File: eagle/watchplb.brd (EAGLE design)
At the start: 100 x 80 mm, 141 parts, among them IC1 SAM-M8Q, IC2 BM70BLES1FC2-0B03AA, Q1 8MHz / LFXTAL020423Reel, Q2 BC817-25SMD, Q3 DMN3023L-7, Q4 16MHz_LFXTAL051370Reel, U1 MCP111-XXXXX/TO, U2 STM32L073RZ, U3 MCP2200-I/SS, U4 TPD3E001DRLR

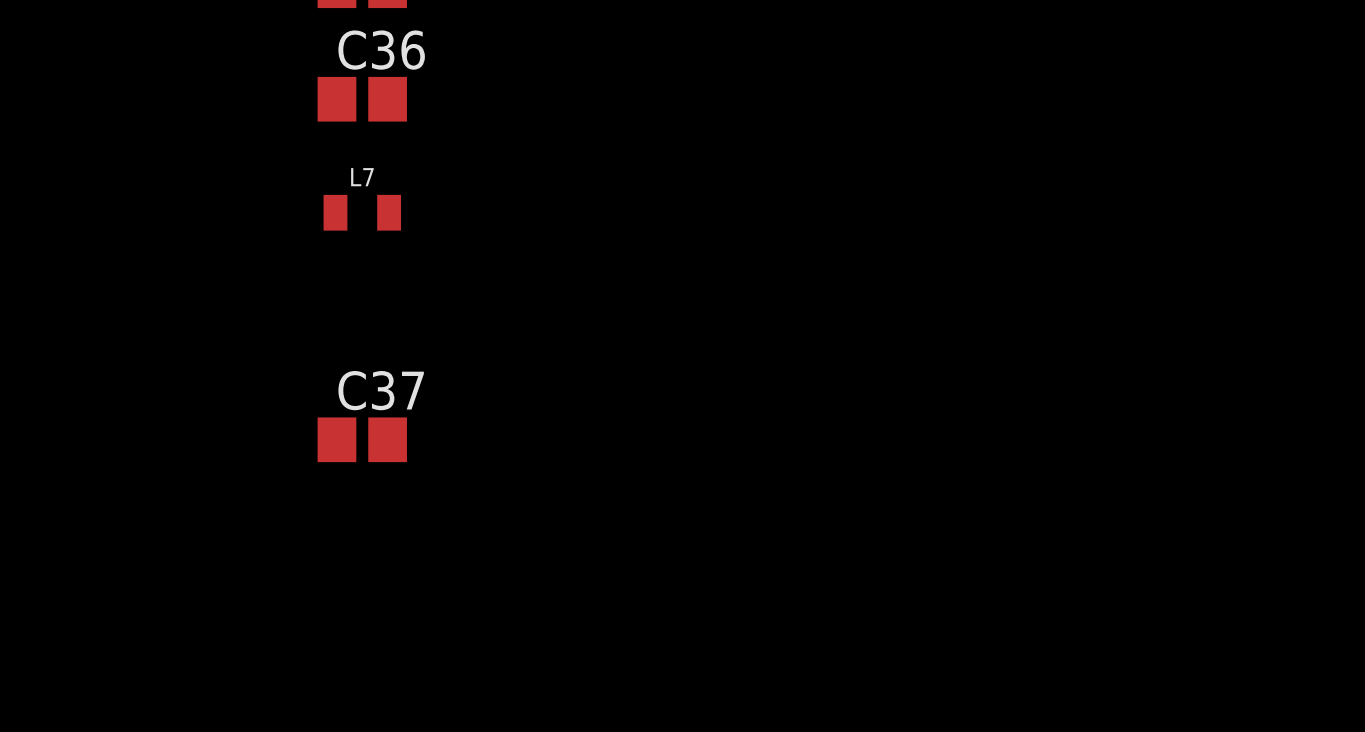
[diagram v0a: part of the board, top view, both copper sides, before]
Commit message: added rf amp and sma connector, reorganised for better pdf page ordering
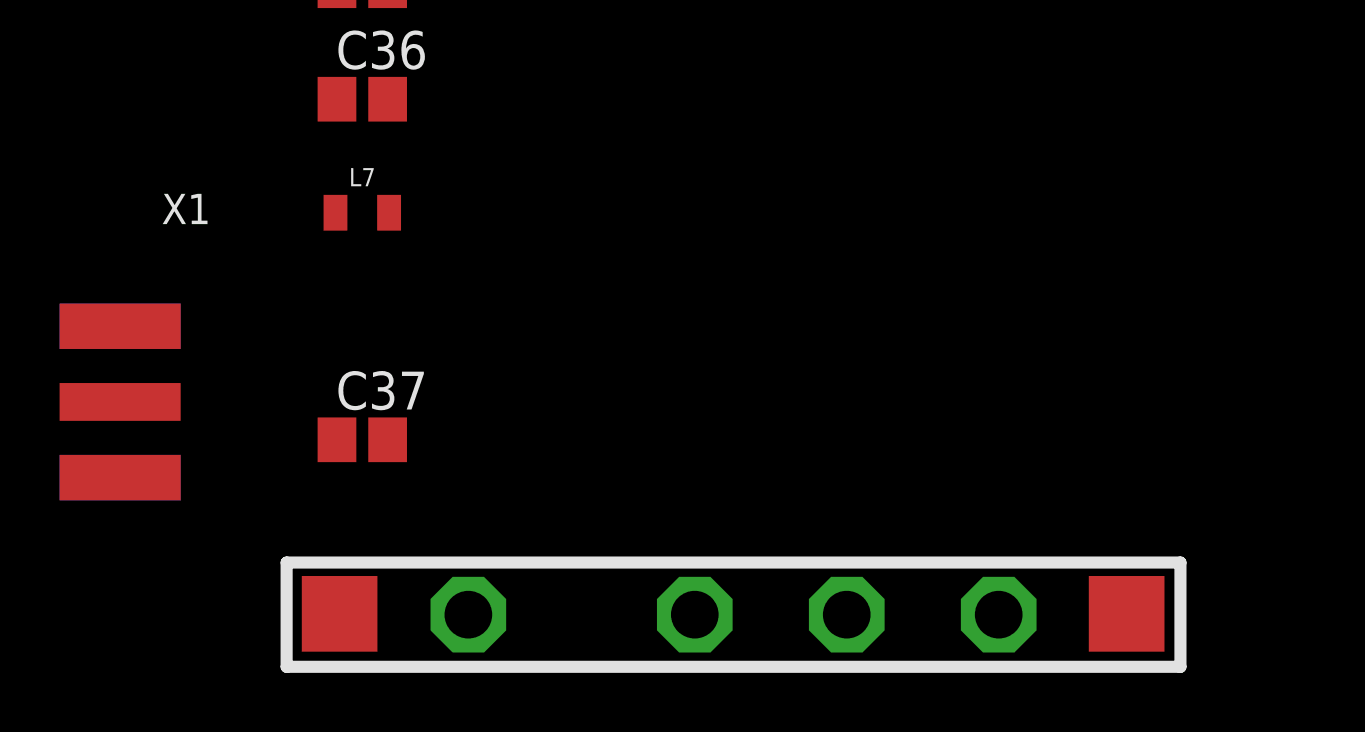
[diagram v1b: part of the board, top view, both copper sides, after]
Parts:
- added U$2: RA07H4047M, Hick:RA07H4047M
- added X1: (no value), adafruit:SMA_EDGELAUNCH
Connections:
- removed net N$38: C24.2, U$1.15
- new net +12V: U$2.2
- new net RF_SIGNAL_AMPLIFIED: U$2.4, X1.P
- net +3V3: now also C24.2, U$1.15, U$2.3
- net GND: now also U$2.5_L, U$2.5_R, X1.GND@1, X1.GND@2, X1.GND@3, X1.GND@4
- net RF_SIGNAL: now also U$2.1
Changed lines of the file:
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@@
 </element>
 <element name="C37" library="resistor" package="C0805" value="" x="-135.89" y="-843.28"/>
+<element name="U$2" library="Hick" package="RA07H4047M" value="RA07H4047M" x="-138.43" y="-850.9"/>
+<element name="X1" library="adafruit" package="SMA_EDGELAUNCH" value="" x="-146.05" y="-842.01"/>
 </elements>
 <signals>
@@
 <contactref element="3V3" pad="TP"/>
 <contactref element="Q2" pad="C"/>
+<contactref element="U$2" pad="3"/>
+<contactref element="U$1" pad="15"/>
+<contactref element="C24" pad="2"/>
 <wire x1="-74.08" y1="-193.04" x2="-67.31" y2="-185.42" width="0" layer="19" extent="1-1"/>
 <wire x1="-81.09" y1="-216.13" x2="-74.08" y2="-193.04" width="0" layer="19" extent="1-1"/>
@@
 <wire x1="-121.92" y1="-521.97" x2="-111.44" y2="-377.19" width="0" layer="19" extent="1-1"/>
 <wire x1="-135.89" y1="-646.6" x2="-121.92" y2="-521.97" width="0" layer="19" extent="1-1"/>
+<wire x1="-135.62" y1="-672.57" x2="-135.89" y2="-646.6" width="0" layer="19" extent="1-1"/>
+<wire x1="-135.04" y1="-698.5" x2="-135.62" y2="-672.57" width="0" layer="19" extent="1-1"/>
+<wire x1="-119.63" y1="-849.15" x2="-135.04" y2="-698.5" width="0" layer="19" extent="1-1"/>
 </signal>
 <signal name="GPS_RXD">
@@
 <contactref element="C36" pad="1"/>
 <contactref element="C37" pad="1"/>
+<contactref element="X1" pad="GND@2"/>
+<contactref element="X1" pad="GND@1"/>
+<contactref element="X1" pad="GND@4"/>
+<contactref element="X1" pad="GND@3"/>
+<contactref element="U$2" pad="5_L"/>
+<contactref element="U$2" pad="5_R"/>
 <wire x1="-74.08" y1="-166.37" x2="-74.08" y2="-172.72" width="0" layer="19" extent="1-1"/>
 <wire x1="-74.93" y1="-185.42" x2="-74.08" y2="-172.72" width="0" layer="19" extent="1-1"/>
@@
 <wire x1="-136.79" y1="-820.42" x2="-136.74" y2="-816.61" width="0" layer="19" extent="1-1"/>
 <wire x1="-136.74" y1="-831.85" x2="-136.79" y2="-820.42" width="0" layer="19" extent="1-1"/>
-<wire x1="-136.74" y1="-843.28" x2="-136.74" y2="-831.85" width="0" layer="19" extent="1-1"/>
+<wire x1="-144.018" y1="-839.47" x2="-136.74" y2="-831.85" width="0" layer="19" extent="1-1"/>
+<wire x1="-144.018" y1="-839.47" x2="-144.018" y2="-839.47" width="0" layer="19" extent="1-16"/>
+<wire x1="-144.018" y1="-844.55" x2="-144.018" y2="-839.47" width="0" layer="19" extent="1-1"/>
+<wire x1="-144.018" y1="-844.55" x2="-144.018" y2="-844.55" width="0" layer="19" extent="1-16"/>
+<wire x1="-136.74" y1="-843.28" x2="-144.018" y2="-844.55" width="0" layer="19" extent="1-1"/>
+<wire x1="-136.652" y1="-849.122" x2="-136.74" y2="-843.28" width="0" layer="19" extent="1-1"/>
+<wire x1="-110.236" y1="-849.122" x2="-136.652" y2="-849.122" width="0" layer="19" extent="1-1"/>
 </signal>
 <signal name="BT_NRST">
@@
 <wire x1="-136.84" y1="-661.67" x2="-134.94" y2="-668.02" width="0" layer="19" extent="1-1"/>
 <wire x1="-136.84" y1="-648.8" x2="-136.84" y2="-661.67" width="0" layer="19" extent="1-1"/>
-</signal>
-<signal name="N$38">
-<contactref element="U$1" pad="15"/>
-<contactref element="C24" pad="2"/>
-<wire x1="-135.62" y1="-672.57" x2="-135.04" y2="-698.5" width="0" layer="19" extent="1-1"/>
 </signal>
 <signal name="INT_POWER">
@@
 <contactref element="L7" pad="2"/>
 <contactref element="C37" pad="2"/>
+<contactref element="U$2" pad="1"/>
+<wire x1="-135.04" y1="-843.28" x2="-132.33" y2="-849.15" width="0" layer="19" extent="1-1"/>
 <wire x1="-134.99" y1="-835.66" x2="-135.04" y2="-843.28" width="0" layer="19" extent="1-1"/>
+</signal>
+<signal name="RF_SIGNAL_AMPLIFIED">
+<contactref element="U$2" pad="4"/>
+<contactref element="X1" pad="P"/>
+<wire x1="-114.53" y1="-849.15" x2="-144.018" y2="-842.01" width="0" layer="19" extent="1-1"/>
+</signal>
+<signal name="+12V">
+<contactref element="U$2" pad="2"/>
 </signal>
 </signals>
 </board>
 </drawing>
+<compatibility>
+<note version="6.3" minversion="6.2.2" severity="warning">
+Since Version 6.2.2 text objects can contain more than one line,
+which will not be processed correctly with this version.
+</note>
+</compatibility>
 </eagle>

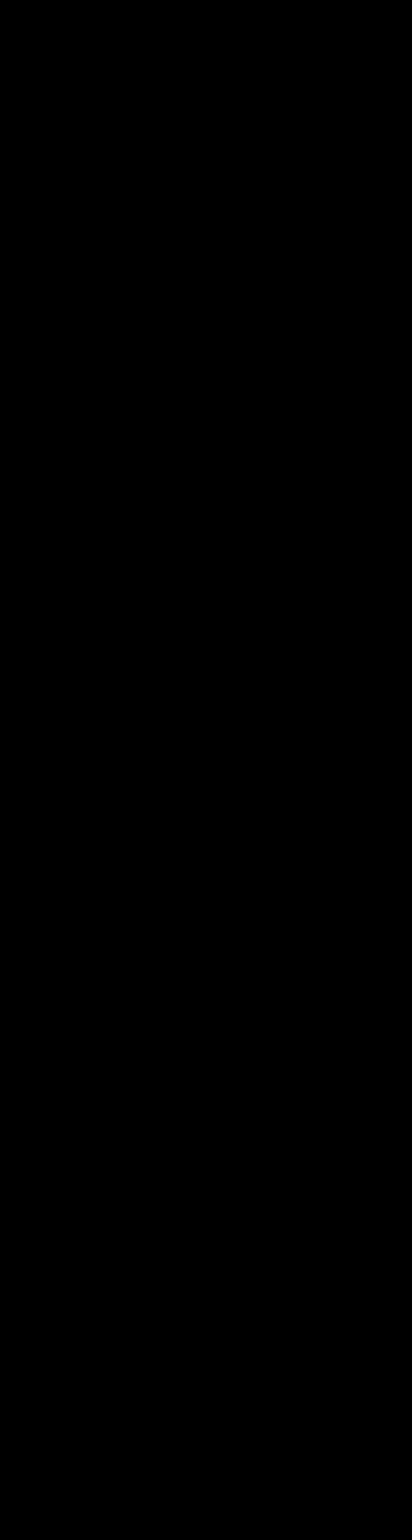
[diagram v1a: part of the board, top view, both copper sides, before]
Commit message: added battery protection circuit
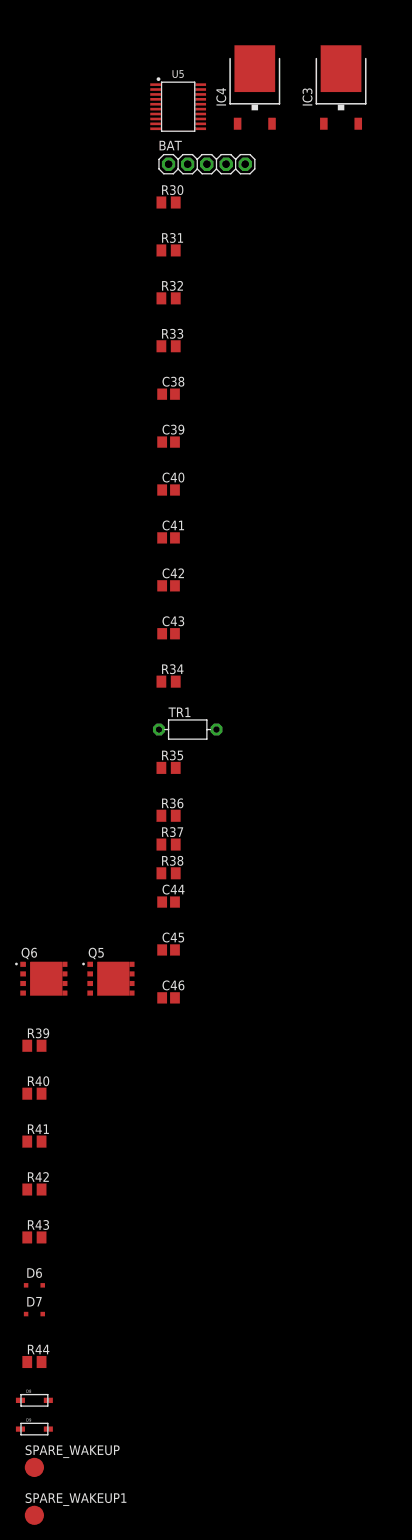
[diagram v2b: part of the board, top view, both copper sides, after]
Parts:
- added BAT: (no value), pinhead:1X05
- added C38, C39, C40, C41, C44, C45, C46: 100nF, resistor:C0805
- added C42, C43: 1uF, resistor:C0805
- added D6: Zener 16V MMSZ5246BS-7-F, diode-1:SOD323-R
- added D7: 100V, BAS16J,135, diode-1:SOD323-R
- added D8, D9: (no value), adafruit:SOD-123
- added IC3: LM1117DTX-ADJ-12V, lm1117:TO252
- added IC4: LM1117DTX-ADJ-3V3, lm1117:TO252
- added Q5, Q6: CSD18534Q5A, CSD18534Q5A:TRANS_CSD18534Q5A
- added R30, R31, R32, R33, R34: 1k, resistor:M0805
- added R35: 10k, resistor:M0805
- added R36: 20mR, resistor:M0805
- added R37, R38: 100R, resistor:M0805
- added R39: 10M, resistor:M0805
- added R40, R43: 5k1, resistor:M0805
- added R41: 3M3, resistor:M0805
- added R42: 1M, resistor:M0805
- added R44: 470k, resistor:M0805
- added SPARE_WAKEUP, SPARE_WAKEUP1: PTR1B2,54, testpad:B2,54
- added TR1: NTC 103AT, discrete:R-7,5
- added U5: BQ7790504, chips:TSSOP-20/6MM
- R10, R11, R14, R15, R18, R19, R20, R21, R22: value 220R -> 470R
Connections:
- removed net V+: D1.C, JP2.1
- new net BAT_PACK_GND: BAT.5, C38.2, C39.2, C40.2, C41.2, C42.1, C43.2, C44.1, C46.2, R36.2, R37.2, TR1.1, U5.18, U5.19, U5.20, U5.8
- new net BAT_PACK_NEG: D6.A, Q6.1, Q6.2, Q6.3, R41.1, R44.2
- new net BAT_PACK_POS: BAT.1, R30.1, R34.1
- new net N$38: R35.2, TR1.2, U5.15
- new net N$46: D6.C, D7.C, Q6.4, R41.2, R42.1
- new net N$47: BAT.2, R31.1
- new net N$48: BAT.3, R32.1
- new net N$49: BAT.4, R33.1
- new net N$50: C39.1, R33.2, U5.7
- new net N$51: C40.1, R32.2, U5.6
- new net N$52: C41.1, R31.2, U5.5
- new net N$53: C38.1, R30.2, U5.3, U5.4
- new net N$54: C43.1, R34.2, U5.1
- new net N$55: Q5.1, Q5.2, Q5.3, R36.1, R38.2, R39.2
- new net N$56: C42.2, U5.17, U5.2
- new net N$57: C45.2, C46.1, R38.1, U5.10
- new net N$58: C44.2, C45.1, R37.1, U5.9
- new net N$59: Q5.5, Q5.6, Q5.7, Q5.8, Q6.5, Q6.6, Q6.7, Q6.8
- new net N$60: R35.1, U5.16
- new net N$62: Q5.4, R39.1, R40.1
- new net N$63: R40.2, U5.11
- new net N$64: D7.A, R42.2, R43.2
- new net N$65: R43.1, U5.13
- new net N$66: R44.1, U5.14
- new net N$67: D8.A, SPARE_WAKEUP1.TP
- new net N$68: D9.A, SPARE_WAKEUP.TP
- net +3V3: now also D1.C, JP2.1
- net MCU_WAKEUP: now also D8.C, D9.C

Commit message: added calculations as excel file and battery charge circuitry in schematic
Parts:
- removed X1: (no value), adafruit:SMA_EDGELAUNCH
- added C47, C49: 100nF, resistor:C0805
- added C48, C51, C52: 22uF 80-EDK226M050A9GAA, rcl:PANASONIC_E
- added C50: 4.7uF, resistor:C0805
- added D10: MBRS330T3, diode:SMC
- added J3: BNCPTH, SparkFun-Connectors:BNC
- added J4: (no value), SparkFun-Connectors:USB-B-MICRO-SMD
- added L8: CTX10-4A-R, CTX10-4A-R:INDM115115X635N
- added Q7: DMN3023L-7, transistor-small-signal:SOT23
- added R45: 330, resistor:M0805
- added R46: 910R, resistor:M0805
- added R47, R49: 10k, resistor:M0805
- added R48: 330k, resistor:M0805
- added R50: 0.25R, resistor:M0805
- added R51: 120k, resistor:M0805
- added R52: 12k4, resistor:M0805
- added U$3: LT1513, Hick:TO220-7
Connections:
- removed net BAT_PACK_NEG: D6.A, Q6.1, Q6.2, Q6.3, R41.1, R44.2
- new net N$61: C50.2, L8.2, U$3.5
- new net N$69: C48.+, J4.VBUS, L8.1, U$3.7
- new net N$70: L8.3, R49.2, R50.2
- new net N$71: C47.2, R45.2
- new net N$72: R45.1, U$3.1
- new net N$73: Q7.3, R46.1
- new net N$74: R46.2, R47.2, R48.1
- new net N$75: C50.1, D10.A, L8.4
- new net N$76: C49.2, R48.2, R49.1, U$3.3
- new net N$77: R51.1, R52.2, U$3.2
- new net S/S: U$3.6
- net +3V3: now also R47.1
- net BAT_PACK_POS: now also C51.+, C52.+, D10.C, R51.2
- net GND: now also C47.1, C48.-, C49.1, C51.-, C52.-, D6.A, J3.GND, J4.GND, J4.SHIELD1, J4.SHIELD2, J4.SHIELD3, Q6.1, Q6.2, Q6.3, Q7.2, R41.1, R44.2, R50.1, R52.1, U$3.4; no longer X1.GND@1, X1.GND@2, X1.GND@3, X1.GND@4
- net RF_SIGNAL_AMPLIFIED: now also J3.S; no longer X1.P

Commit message: added linear regulators + calculations for them, exported parts as library, generated new pdf
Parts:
- removed IC4: LM1117DTX-ADJ-3V3, lm1117:TO252
- added B1, B2, B3, B4, B5, B6, B7: BLM18KG601SN1D, PCB4_Demoboard:L0603
- added C53, C56, C59: 10uF 80-EDK106M025A9DAA, rcl:PANASONIC_E
- added C54, C57, C60: 100uF 647-GYA1E101MCQ1GS, rcl:PANASONIC_E
- added C55, C58, C61: NP, rcl:PANASONIC_E
- added IC5: LM1117DTX-ADJ-10V, lm1117:TO252
- added IC6: LM1117DTX-ADJ-3V3, lm1117:TO252
- added JP3: Power Disconnect, pinhead:1X02
- added R53, R55, R57: 5k1, resistor:M0805
- added R54, R56, R58: 47k, resistor:M0805
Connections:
- new net 10V_INTERMEDIATE: C57.+, C59.+, IC5.TAB, IC6.2, R55.1
- new net N$78: B4.2, CONFIG_INTERFACE_TEST_POINT.2
- new net N$79: B2.2, C1.1, C2.1, C3.1, IC1.17, IC1.2, IC1.3, R1.1, R2.1
- new net N$80: B3.2, IC2.4, LED1.A, R3.1, U1.3
- new net N$81: B5.2, D1.C, JP2.1
- new net N$82: B6.2, C24.2, U$1.15
- new net N$83: B7.2, U$2.3
- new net N$84: C53.+, C56.+, IC3.2, IC5.2, JP3.2
- new net N$85: C55.+, IC3.1, R53.2, R54.1
- new net N$89: C58.+, IC5.1, R55.2, R56.1
- new net N$92: C61.+, IC6.1, R57.2, R58.1
- new net V+STM: B1.2, C10.2, C16.2, C4.1, C5.2, C6.2, C8.1, C9.1, U2.1, U2.13, U2.19, U2.32, U2.64
- net +12V: now also C54.+, IC3.TAB, R53.1
- net +3V3: now also B1.1, B2.1, B3.1, B4.1, B5.1, B6.1, B7.1, C60.+, IC6.TAB, R57.1; no longer C1.1, C10.2, C16.2, C2.1, C24.2, C3.1, C4.1, C5.2, C6.2, C8.1, C9.1, CONFIG_INTERFACE_TEST_POINT.2, D1.C, IC1.17, IC1.2, IC1.3, IC2.4, JP2.1, LED1.A, R1.1, R2.1, R3.1, U$1.15, U$2.3, U1.3, U2.1, U2.13, U2.19, U2.32, U2.64
- net BAT_PACK_POS: now also JP3.1
- net GND: now also C53.-, C54.-, C55.-, C56.-, C57.-, C58.-, C59.-, C60.-, C61.-, R54.2, R56.2, R58.2

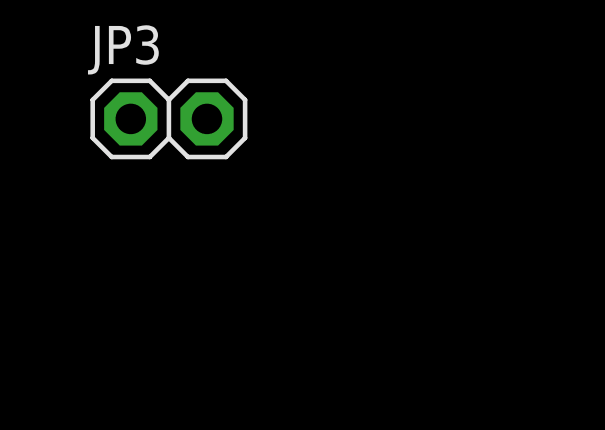
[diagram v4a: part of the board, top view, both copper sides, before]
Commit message: added 4.7uF to gps module because the devboard does that.
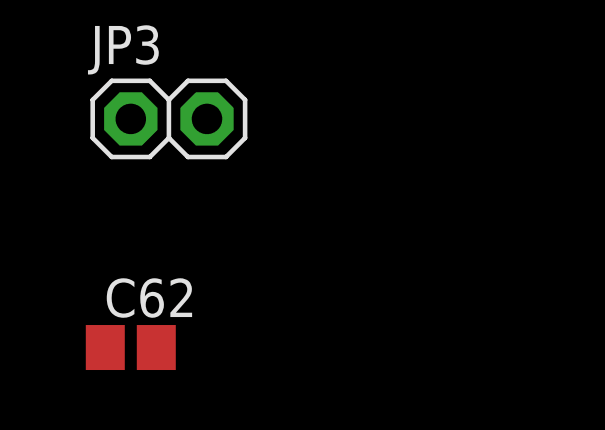
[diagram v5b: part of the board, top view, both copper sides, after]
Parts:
- added C62: 4.7uF, resistor:C0805
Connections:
- net GND: now also C62.2
- net N$79: now also C62.1
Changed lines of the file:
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@@
 <element name="C61" library="rcl" package="PANASONIC_E" value="NP" x="-241.3" y="175.26"/>
 <element name="JP3" library="pinhead" package="1X02" value="Power Disconnect" x="-242.57" y="-1234.44"/>
+<element name="C62" library="resistor" package="C0805" value="4.7uF" x="-243.84" y="-1242.06"/>
 </elements>
 <signals>
@@
 <contactref element="C60" pad="-"/>
 <contactref element="C61" pad="-"/>
+<contactref element="C62" pad="2"/>
 <wire x1="-74.08" y1="-166.37" x2="-74.08" y2="-172.72" width="0" layer="19" extent="1-1"/>
 <wire x1="-74.93" y1="-185.42" x2="-74.08" y2="-172.72" width="0" layer="19" extent="1-1"/>
@@
 <wire x1="-242.89" y1="-1217.93" x2="-244.3" y2="-1203.96" width="0" layer="19" extent="1-1"/>
 <wire x1="-244.3" y1="-1225.55" x2="-242.89" y2="-1217.93" width="0" layer="19" extent="1-1"/>
+<wire x1="-242.99" y1="-1242.06" x2="-244.3" y2="-1225.55" width="0" layer="19" extent="1-1"/>
 <wire x1="-227.65" y1="124.46" x2="-43.18" y2="-21.59" width="0" layer="19" extent="1-1"/>
 <wire x1="-244.3" y1="125.73" x2="-227.65" y2="124.46" width="0" layer="19" extent="1-1"/>
@@
 <contactref element="R1" pad="1"/>
 <contactref element="R2" pad="1"/>
-<wire x1="54.86" y1="46.35" x2="-242.99" y2="-1162.05" width="0" layer="19" extent="1-16"/>
+<contactref element="C62" pad="1"/>
+<wire x1="-242.99" y1="-1162.05" x2="-244.69" y2="-1242.06" width="0" layer="19" extent="1-1"/>
+<wire x1="54.86" y1="46.35" x2="-244.69" y2="-1242.06" width="0" layer="19" extent="1-16"/>
 <wire x1="54.86" y1="44.45" x2="54.86" y2="46.35" width="0" layer="19" extent="16-16"/>
 <wire x1="46.36" y1="51.05" x2="54.86" y2="46.35" width="0" layer="19" extent="16-16"/>

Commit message: small schematic changes, started with layout
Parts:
- removed SPARE_WAKEUP, SPARE_WAKEUP1, USB_5V, USB_D+, USB_D-: PTR1B2,54, testpad:B2,54
- removed TR1: NTC 103AT, discrete:R-7,5
- added BAT_ADC, RF_SIGNAL: PTR1B2,54, testpad:B2,54
- added R59, R61: 10k, resistor:M0805
- added R60: 47k, resistor:M0805
- added R62: NTC 103AT, resistor:M0805
- C38, C39, C40, C41, C42, C43, C44, C45, C46, C47, C49, C50, C62: device resistor:C0805 -> resistor:C0805K
- R36: device resistor:M0805 -> resistor:R2512
- moved B3 1328.4 mm to (-0.91, 138.8)
- moved B4 1327.7 mm to (-9.91, 134.7)
- moved B2 1313.9 mm to (-100.9, 144.0)
- moved JP3 1312.9 mm to (-209.6, 78.0)
- moved C55 1286.1 mm to (-231.5, 60.5), turned to 90 degrees
- moved R54 1285.2 mm to (-220.1, 67.1)
- moved R53 1278.0 mm to (-228.3, 66.3), turned to 270 degrees
- moved C54 1271.0 mm to (-237.9, 67.1)
- moved C53 1255.7 mm to (-222.8, 60.5), turned to 90 degrees
- moved B1 1107.3 mm to (-108.8, -57.9)
- moved B6 1104.1 mm to (-349.9, -83.4)
- moved B7 1097.4 mm to (-298.9, -91.4)
- moved B5 1079.0 mm to (12.0, -129.1), turned to 270 degrees
- moved D9 953.7 mm to (5.79, -92.8), turned to 270 degrees
- moved C62 952.2 mm to (-307.8, -292.0)
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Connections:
- removed net S/S: U$3.6
- new net BAT_ADC: BAT_ADC.TP, R60.1, R61.2, U2.15
- new net CHARGER_CH_PRECH: Q7.1, U2.54
- new net CHARGER_SS: U$3.6, U2.53
- new net N$86: C11.2, R59.1
- net +3V3: now also R1.1, R2.1
- net +5V: no longer USB_5V.TP
- net BAT_PACK_GND: now also R62.2; no longer TR1.1
- net GND: now also R61.1
- net N$17: no longer USB_D-.TP
- net N$20: no longer USB_D+.TP
- net N$38: now also R62.1; no longer TR1.2
- net N$67: no longer SPARE_WAKEUP1.TP
- net N$68: no longer SPARE_WAKEUP.TP
- net N$79: no longer R1.1, R2.1
- net N$84: now also R60.2
- net NRST: now also R59.2; no longer C11.2
- net RF_SIGNAL: now also RF_SIGNAL.TP
- net USB_DATA_NEG: now also U4.1; no longer U4.2
- net USB_DATA_POS: now also U4.2; no longer U4.1
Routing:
- net GND: track 0.00 -> 222.0 mm, vias 0 -> 4
- net +3V3: track 0.00 -> 149.2 mm
- net BTN_1: track 0.00 -> 65.5 mm
- net BAT_PACK_GND: track 0.00 -> 62.5 mm
- net BTN_2: track 0.00 -> 51.4 mm
- net BTN_3: track 0.00 -> 37.2 mm
- net MCU_WAKEUP: track 0.00 -> 29.6 mm
- net +5V: track 0.00 -> 24.5 mm
- net NRST: track 0.00 -> 24.5 mm
- net BTN_4: track 0.00 -> 22.8 mm
- net N$85: track 0.00 -> 22.7 mm
- net N$89: track 0.00 -> 22.6 mm
- net 10V_INTERMEDIATE: track 0.00 -> 21.2 mm
- net N$62: track 0.00 -> 21.1 mm, vias 0 -> 2
- net N$92: track 0.00 -> 19.2 mm
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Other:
- board size 100 x 80 mm -> 100 x 100 mm
